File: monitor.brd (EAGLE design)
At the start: 148.1 x 84.8 mm, 72 parts, among them IC1 LM1117-5, IC2 LM1117-5, J3 DCJ0202, J4 DCJ0202, J5 DCJ0202, Q1 IRLML2502, T1 BC846, T2 BT148, X3 PN61729-S, X4 PN87520-S

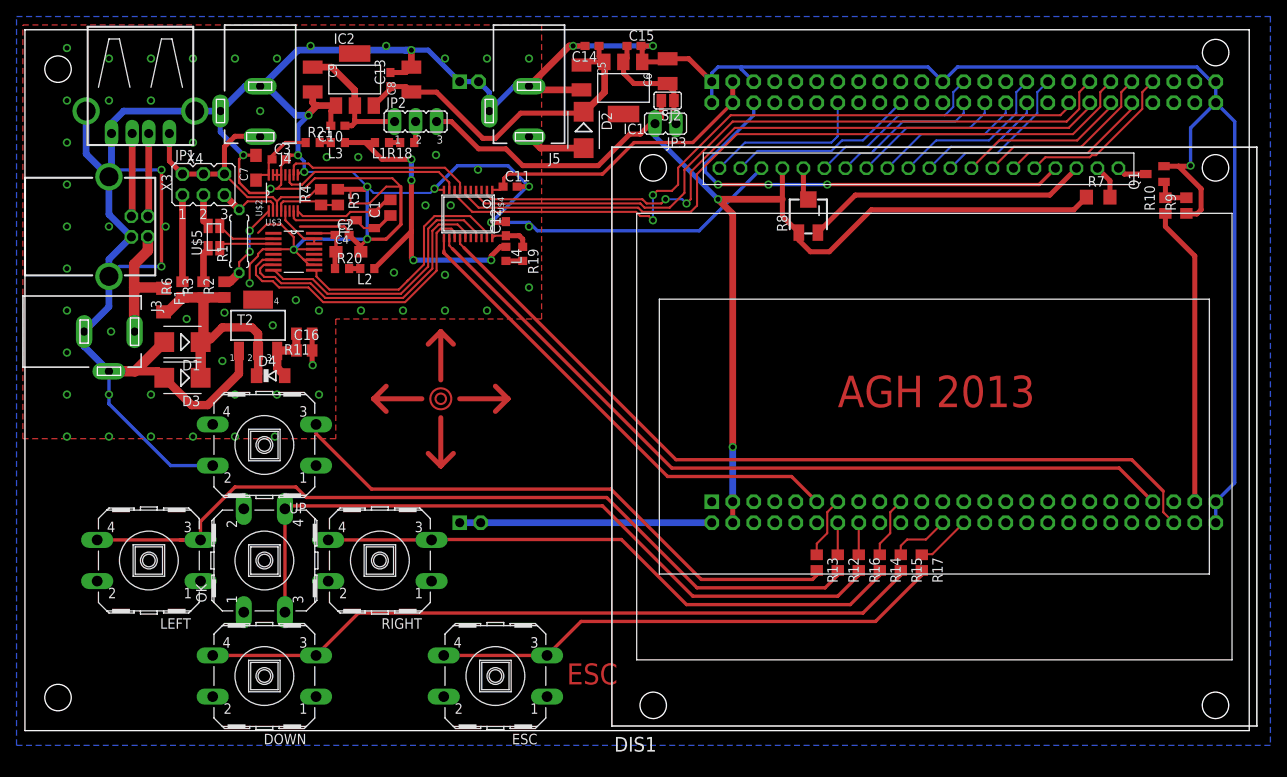
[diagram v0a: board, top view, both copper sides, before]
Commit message: Ground plane on top layer
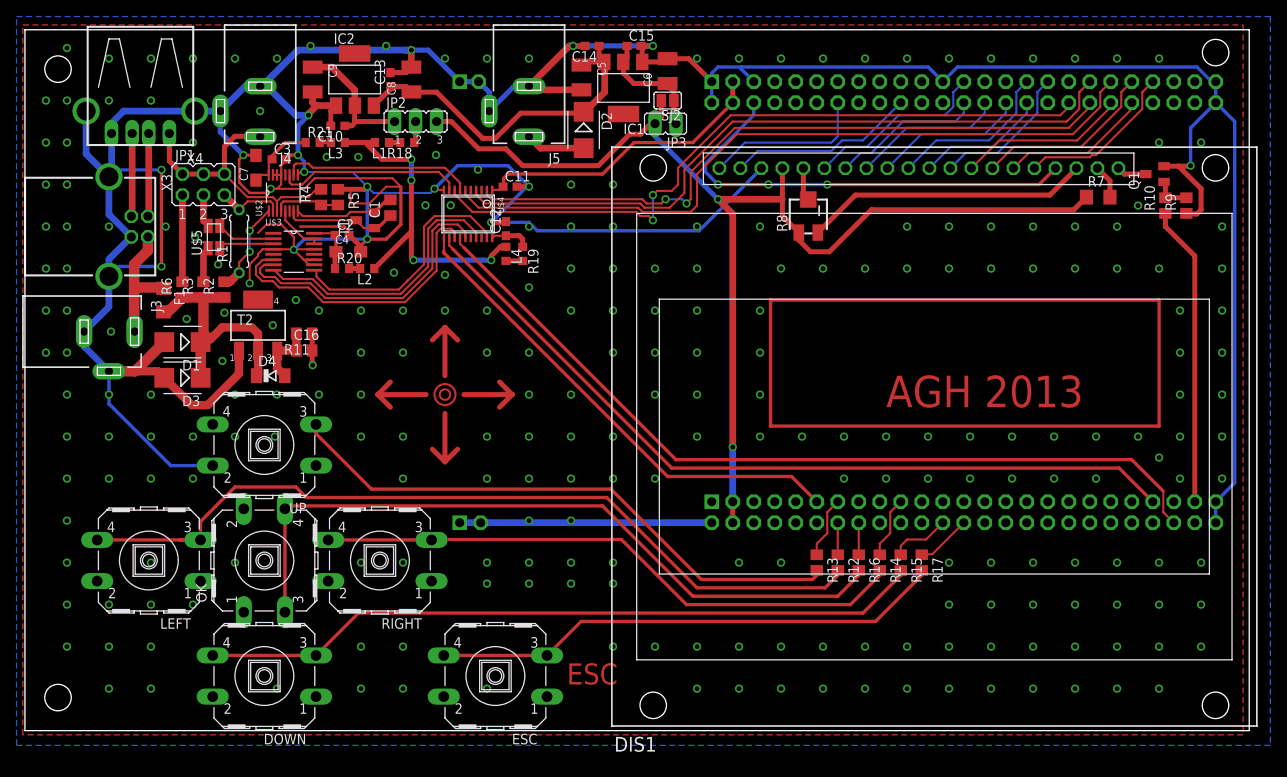
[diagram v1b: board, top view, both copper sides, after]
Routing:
- net N$34: track 0.00 -> 124.5 mm
- net GND: vias 76 -> 266

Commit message: RMT
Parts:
- moved L1 0.25 mm to (43.2, 70.9)
- moved R18 0.25 mm to (46.2, 70.9)
- moved L4 0.25 mm to (58.2, 57.4)
- moved R19 0.25 mm to (60.2, 57.4)
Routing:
- net VCC: track 40.8 -> 39.2 mm
- net GND: track 611.7 -> 611.0 mm, vias 266 -> 267

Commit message: vias
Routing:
- net GND: vias 267 -> 270
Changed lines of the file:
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@@
 <setting verticaltext="up"/>
 </settings>
-<grid distance="10" unitdist="mil" unit="mil" style="lines" multiple="1" display="yes" altdistance="1" altunitdist="mil" altunit="mil"/>
+<grid distance="200" unitdist="mil" unit="mil" style="lines" multiple="1" display="yes" altdistance="10" altunitdist="mil" altunit="mil"/>
 <layers>
 <layer number="1" name="Top" color="4" fill="1" visible="yes" active="yes"/>
@@
 <wire x1="26.924" y1="65.278" x2="26.416" y2="65.786" width="0.254" layer="1"/>
 <wire x1="26.416" y1="65.786" x2="26.416" y2="69.596" width="0.254" layer="1"/>
+<via x="71.12" y="72.39" extent="1-16" drill="0.6"/>
+<via x="72.136" y="77.216" extent="1-16" drill="0.6"/>
+<via x="71.12" y="82.804" extent="1-16" drill="0.6"/>
 </signal>
 <signal name="SPI2_NSS">

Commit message: condensators, minor layout changes
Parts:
- added C17: 10u, rcl:C1206
- added C18, C19: 100n, rcl:C0603
- F1: value 500m -> 1A
- moved D1 3.25 mm to (17.0, 44.5), turned to 270 degrees
- moved D3 2.70 mm to (21.1, 44.5), turned to 270 degrees
- moved R9 1.70 mm to (138.9, 64.3), turned to 180 degrees
- moved R10 1.63 mm to (138.9, 62.2), turned to 180 degrees
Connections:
- net +5V: now also C17.1
- net B_ESC: now also U$1.P$80; no longer U$1.P$76
- net GND: now also C17.2, C18.2, C19.2
- net N$13: now also C19.1
- net OUT: now also C18.1
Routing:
- net GND: track 611.0 -> 584.1 mm, vias 270 -> 277
- net B_ESC: track 6.69 -> 11.8 mm
- net OUT: track 33.6 -> 36.0 mm
- net SPI2_MISO: track 81.8 -> 79.9 mm
- net +5V: track 142.0 -> 143.7 mm
- net SPI2_NSS: track 85.3 -> 83.7 mm
- net SPI2_MOSI: track 89.4 -> 88.0 mm
- net LCD_LED: track 36.3 -> 35.2 mm
- net N$13: track 31.0 -> 31.9 mm
- net SPI2_SCK: track 84.6 -> 83.7 mm
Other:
- board text added: "AGH 2014"
- board text removed: "AGH 2013"
